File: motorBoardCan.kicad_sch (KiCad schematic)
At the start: 31 parts, among them J1 Conn_01x04_Pin, J2 Conn_01x04_Pin, J3 Conn_02x04_Top_Bottom, J6 Conn_02x04_Top_Bottom, U1 NUCLEO-G431KB, U2 XGZP160-SOP_pressure_sensor, U3 XGZP160-SOP_pressure_sensor, U4 SN65HVD230, U5 LD1117S33TR_SOT223

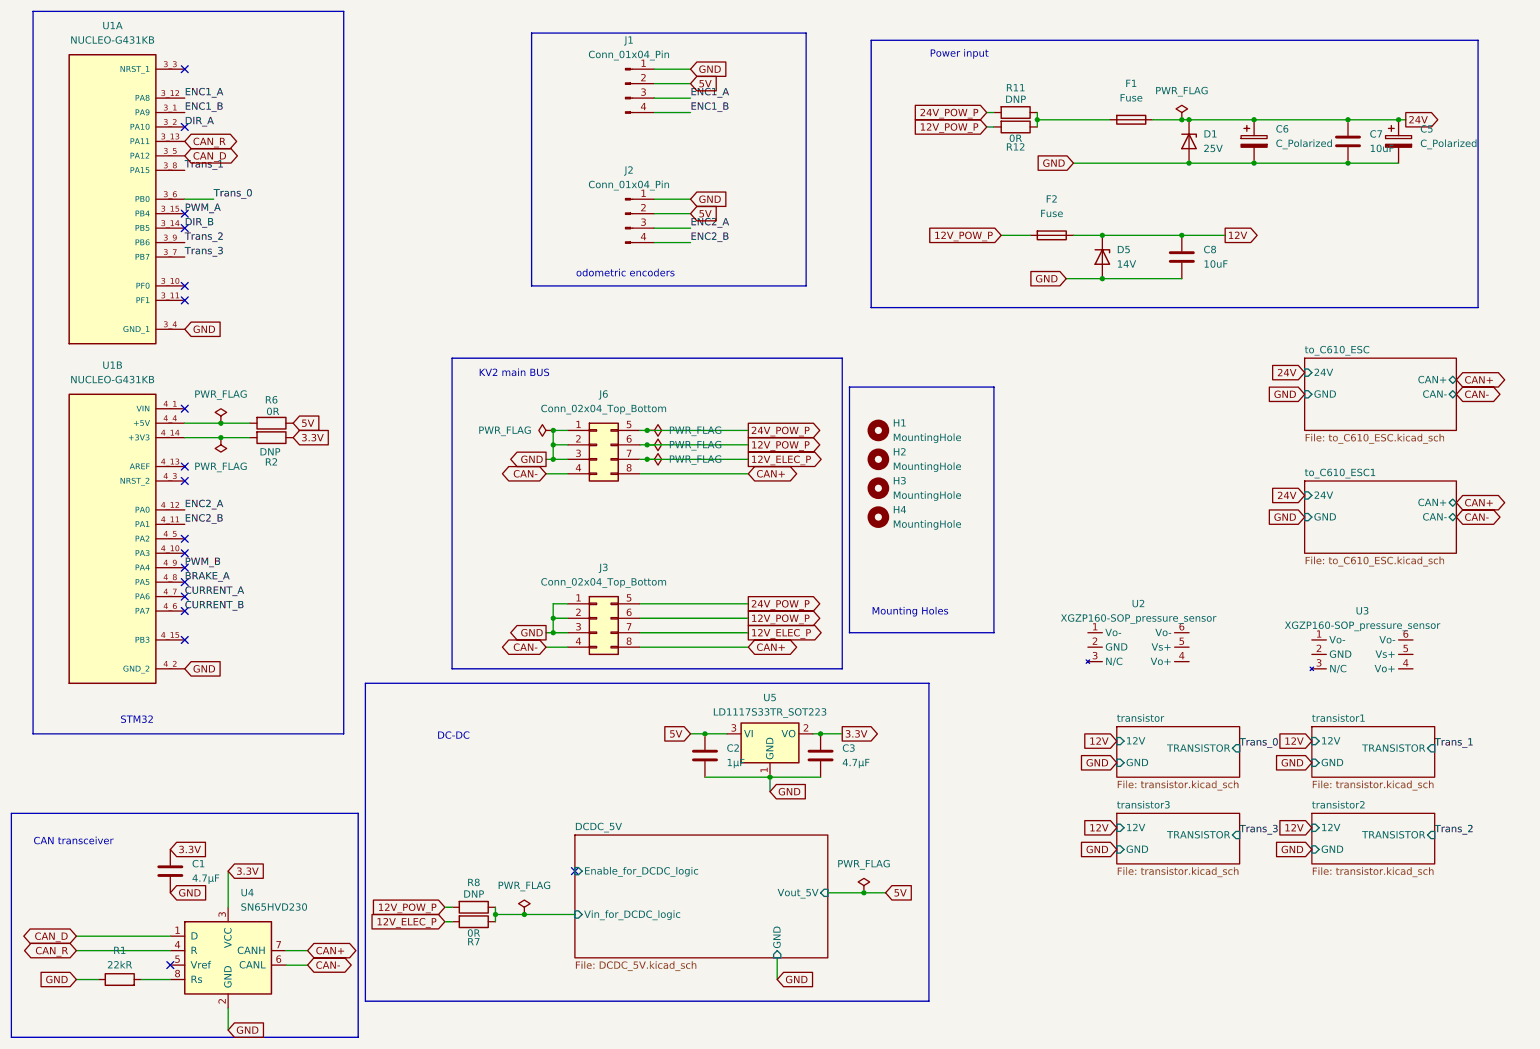
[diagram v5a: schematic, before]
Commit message: remove pressure measure, add voltage measure, re-route
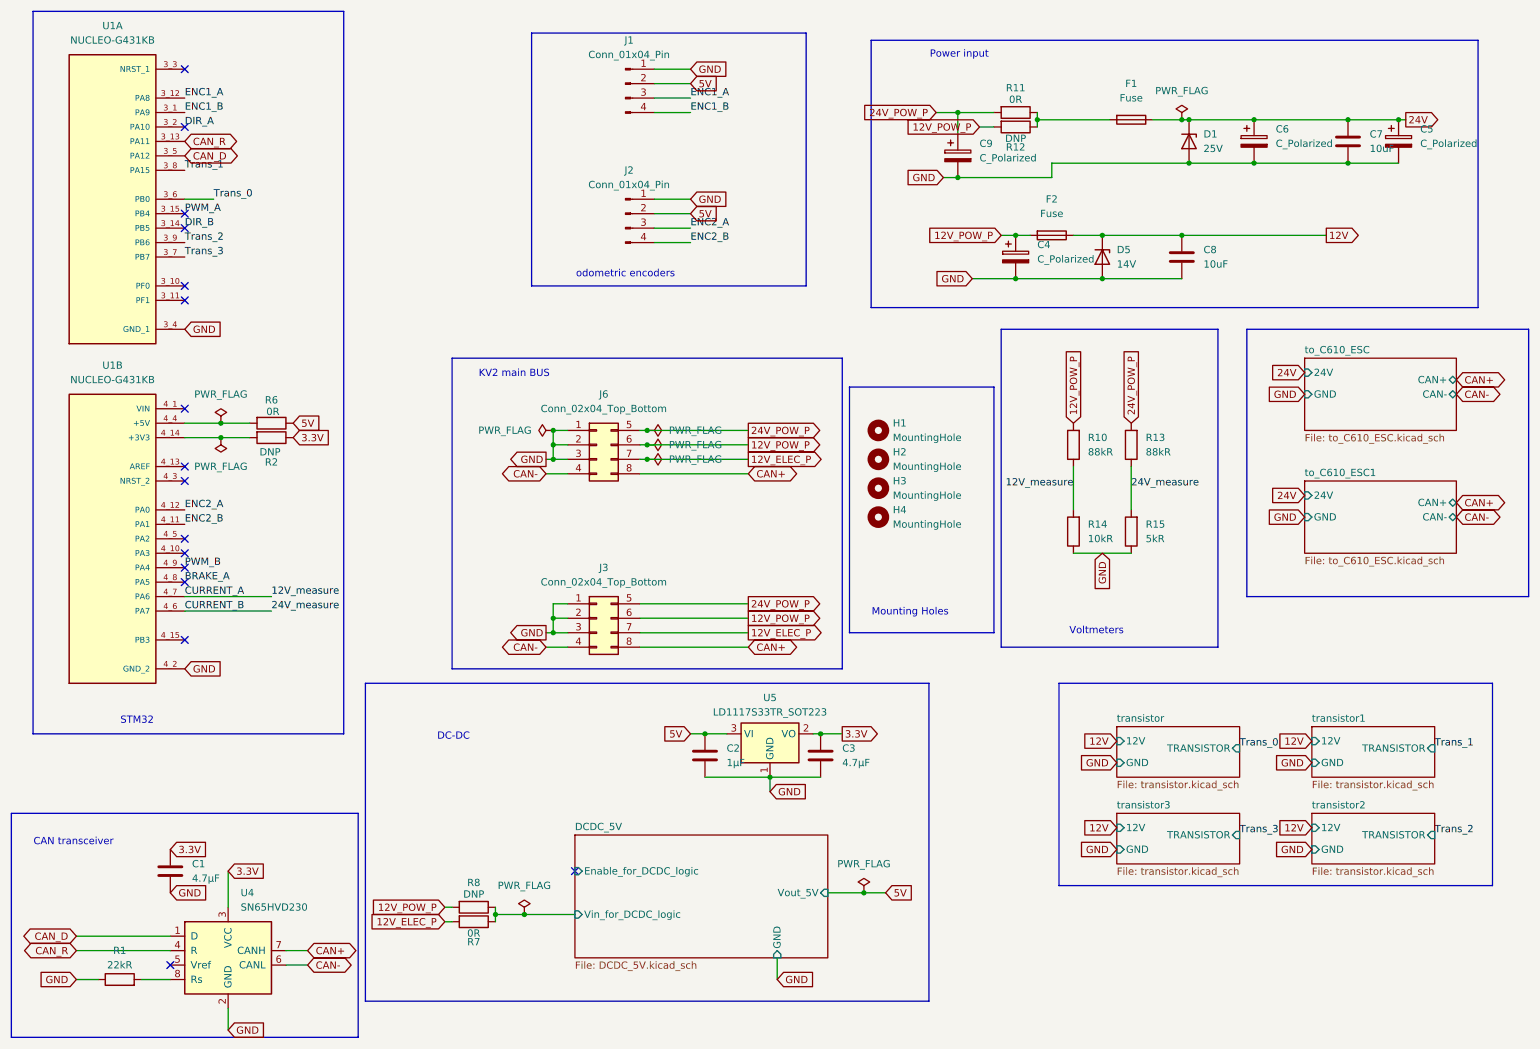
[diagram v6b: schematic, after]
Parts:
- removed U2, U3: XGZP160-SOP_pressure_sensor, LibraryVictor2026:XGZP160-SOP, symbol New_Library_Victor:XGZP160-SOP_pressure_sensor
- added C4, C9: C_Polarized, Capacitor_SMD:CP_Elec_10x10.5, symbol Device:C_Polarized
- added R10, R13: 88kR, Resistor_SMD:R_0603_1608Metric, symbol Device:R
- added R14: 10kR, Resistor_SMD:R_0603_1608Metric, symbol Device:R
- added R15: 5kR, Resistor_SMD:R_0603_1608Metric, symbol Device:R
- R11: value DNP -> 0R
- R12: value 0R -> DNP
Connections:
- net 12V_POW_P: now also C4.1, R10.2
- net 24V_POW_P: now also C9.1, R13.2
- net GND: now also C4.2, C9.2, R14.1, R15.1
- net CURRENT_A renamed 12V_measure
- net 12V_measure: now also R10.1, R14.2
- net CURRENT_B renamed 24V_measure
- net 24V_measure: now also R13.1, R15.2
- no-connect marks 18 -> 16
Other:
- note added: "Voltmeters"

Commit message: bigger jumper resistors
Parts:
- R11, R12: footprint Resistor_SMD:R_0603_1608Metric -> Resistor_SMD:R_1206_3216Metric
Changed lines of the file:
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@@
 			)
 		)
-		(property "Footprint" "Resistor_SMD:R_0603_1608Metric"
+		(property "Footprint" "Resistor_SMD:R_1206_3216Metric"
 			(at 190.5 29.972 90)
 			(hide yes)
@@
 			)
 		)
-		(property "Footprint" "Resistor_SMD:R_0603_1608Metric"
+		(property "Footprint" "Resistor_SMD:R_1206_3216Metric"
 			(at 190.5 27.432 90)
 			(hide yes)
